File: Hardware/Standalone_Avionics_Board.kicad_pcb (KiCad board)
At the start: 4 copper layers, 112.4 x 57.1 mm, 131 parts, among them J1 GPS_Ant, J2 Charges A/B Terminal, J3 Charges C/D Terminal, J4 RF_Ant, J5 3-Pin Molex Power, J6 10118192-0001LF, J7 ARM 10 Pin, Q1 SI1040X-T1-GE3, Q2 SI7232DN-T1-GE3, Q3 SI7232DN-T1-GE3, U1 Si4463, U10 LM317T, U11 USBLC6-2SC6, U12 STM32L562VET, U13 W25Q32JVSS, U2 Si4463, U3 RSD-897.500-942.500-1612-TR, U4 ADL5521, U5 MS5607-02BA, U6 MAX-8Q, U7 KX134-1211, U8 MCP9808_MSOP, U9 BNO055, Y1 30MHz, Y2 30MHz, Y3 32.768kHz

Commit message: Routed ESD protection chip for USB
I really hate how this connects, I made the chip go on the bottom of the board but I really don't want to
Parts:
- added REF**: PinSocket_1x04_P2.54mm_Vertical, Connector_PinSocket_2.54mm:PinSocket_1x04_P2.54mm_Vertical, F.Cu at (4.42, -6.05)
- added REF**: PinHeader_1x04_P2.54mm_Vertical, Connector_PinHeader_2.54mm:PinHeader_1x04_P2.54mm_Vertical, F.Cu at (4.42, -27.9)
- added REF**: PinHeader_1x05_P2.54mm_Vertical, Connector_PinHeader_2.54mm:PinHeader_1x05_P2.54mm_Vertical, B.Cu at (113.0, 163.3)
- added REF**: PinSocket_1x05_P2.54mm_Vertical, Connector_PinSocket_2.54mm:PinSocket_1x05_P2.54mm_Vertical, B.Cu at (113.0, 141.5)
- added REF**: PinSocket_1x05_P2.54mm_Vertical, Connector_PinSocket_2.54mm:PinSocket_1x05_P2.54mm_Vertical, F.Cu at (113.0, 131.5)
- added REF**: PinHeader_1x05_P2.54mm_Vertical, Connector_PinHeader_2.54mm:PinHeader_1x05_P2.54mm_Vertical, F.Cu at (113.0, 109.7)
- C23, L12, Q1, R2, R3, R4, U11: moved to B.Cu
- Y3: footprint Crystal:Crystal_DS26_D2.0mm_L6.0mm_Horizontal_1EP_style1 -> Crystal:Crystal_SMD_0603-2Pin_6.0x3.5mm
- moved R2 215.7 mm to (99.7, 149.3), turned to 315 degrees
- moved R3 214.8 mm to (103.7, 148.9), turned to 135 degrees
- moved C23 212.6 mm to (104.2, 146.8), turned to 45 degrees
- moved Q1 212.3 mm to (101.3, 146.7), turned to 315 degrees
- moved L12 211.0 mm to (101.5, 149.7), turned to 270 degrees
- moved R4 208.2 mm to (103.3, 145.4), turned to 315 degrees
- moved FB1 112.3 mm to (154.3, 109.1)
- moved C28 87.9 mm to (166.9, 131.1), turned to 180 degrees
- moved C27 87.2 mm to (150.9, 127.9), turned to 180 degrees
- moved C26 85.8 mm to (155.0, 125.2), turned to 180 degrees
- moved C29 76.9 mm to (167.1, 128.2)
- moved J6 65.1 mm to (169.1, 110.5)
- moved U11 46.2 mm to (157.3, 110.1), turned to 0 degrees
- moved Y3 11.1 mm to (163.9, 129.6)
- moved C35 7.81 mm to (142.9, 124.5), turned to 45 degrees
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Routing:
- net /USB, ESD, and Debug/D-: track 0.00 -> 41.0 mm, vias 0 -> 1
- net /USB, ESD, and Debug/D+: track 0.00 -> 40.5 mm, vias 0 -> 1
- net /~GPS_RESET: track 0.00 -> 35.2 mm
- net GND: track 40.3 -> 66.9 mm, vias 10 -> 23
- net /GPS_TX: track 0.00 -> 25.6 mm
- net /GPS_RX: track 0.00 -> 15.4 mm
- net /USB, ESD, and Debug/USB_CONN_D+: track 0.00 -> 13.7 mm, vias 0 -> 1
- net +3V3: track 26.3 -> 39.5 mm, vias 6 -> 8
- net Net-(C28-Pad2): track 0.00 -> 12.5 mm
- net /USB, ESD, and Debug/USB_CONN_D-: track 0.00 -> 11.9 mm, vias 0 -> 1
- net /MAX-8Q/GPS_ANT: track 0.00 -> 11.8 mm
- net Net-(C29-Pad1): track 0.00 -> 11.2 mm
- net /SENSORS_I2C_SDA: track 23.0 -> 31.4 mm
- net /MAX-8Q/GPS_VCC_RF: track 0.00 -> 7.46 mm
- net /SENSORS_I2C_SCL: track 28.3 -> 34.5 mm
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- added copper zone on GND.Cu, net GND

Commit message: All chips on layout besides passives
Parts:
- removed the REF** at (4.42, -6.05)
- removed the REF** at (4.42, -27.9)
- U10: footprint Package_TO_SOT_THT:TO-220-3_Vertical -> Package_TO_SOT_SMD:SOT-223-3_TabPin2
- moved C45 150.5 mm to (146.6, 116.6), turned to 90 degrees
- moved R6 133.9 mm to (157.3, 116.0)
- moved R17 127.7 mm to (173.0, 165.9)
- moved R5 124.1 mm to (159.2, 116.0)
- moved R16 121.4 mm to (139.2, 152.0)
- moved U10 119.2 mm to (156.7, 112.0), turned to 180 degrees
- moved C31 118.6 mm to (163.2, 114.2), turned to 270 degrees
- moved R20 118.3 mm to (173.9, 163.0)
- moved R18 116.0 mm to (170.0, 165.4)
- moved R15 114.3 mm to (172.8, 146.9)
- moved R22 111.8 mm to (168.7, 161.5)
- moved R19 108.4 mm to (168.2, 144.7)
- moved R21 108.3 mm to (179.1, 145.2)
- moved R26 108.3 mm to (163.2, 156.2)
- moved R28 108.3 mm to (176.2, 145.2)
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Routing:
- net +5V: track 0.00 -> 28.0 mm, vias 0 -> 1
- net /USB, ESD, and Debug/D-: track 41.0 -> 16.6 mm
- net /USB, ESD, and Debug/D+: track 40.5 -> 17.9 mm
- net +3V3: track 39.5 -> 60.3 mm, vias 8 -> 12
- net GND: track 66.9 -> 81.8 mm, vias 23 -> 31
- net /FLASH_MOSI: track 0.00 -> 14.0 mm
- net /~FLASH_CS: track 0.00 -> 13.2 mm
- net /GPS_RX: track 15.4 -> 28.2 mm
- net /FLASH_MISO: track 0.00 -> 12.7 mm
- net /USB, ESD, and Debug/USB_CONN_D+: track 13.7 -> 26.1 mm
- net /USB, ESD, and Debug/USB_CONN_D-: track 11.9 -> 24.3 mm
- net /FLASH_CLK: track 0.00 -> 12.1 mm
- net Net-(R5-Pad1): track 0.00 -> 3.12 mm
- net Net-(FB1-Pad2): track 0.00 -> 2.46 mm
- net Net-(D1-Pad2): track 0.00 -> 1.09 mm

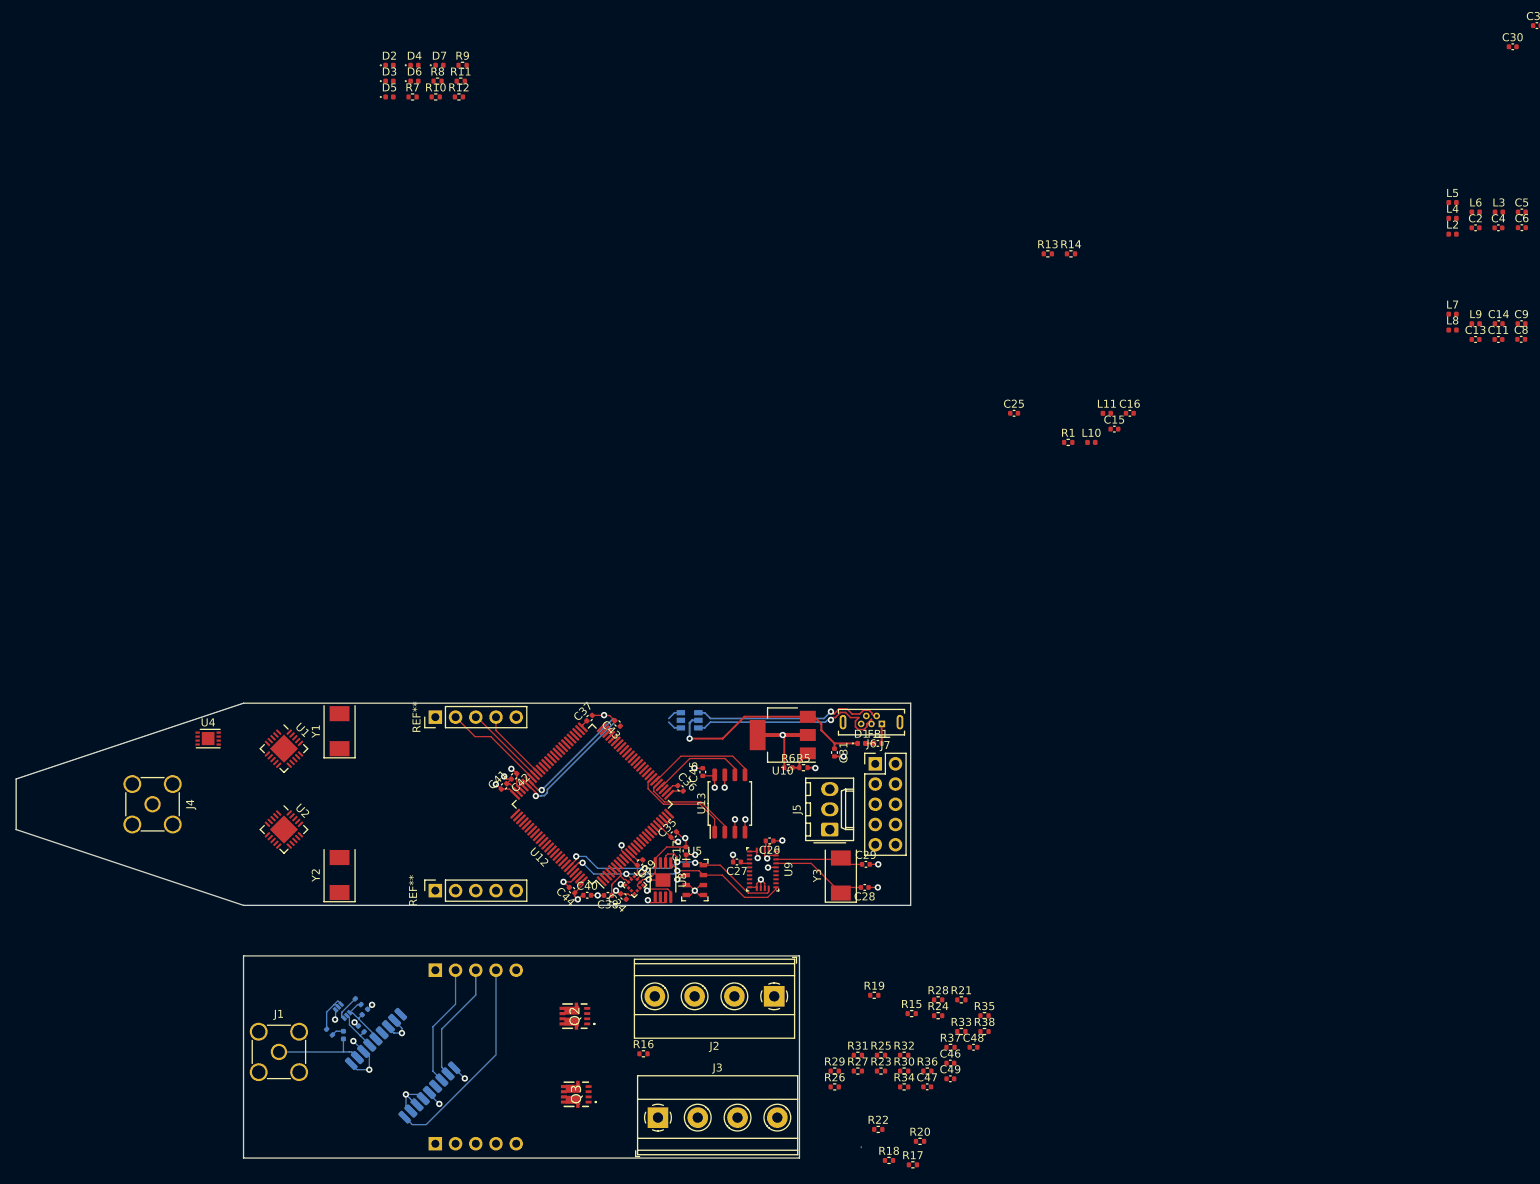
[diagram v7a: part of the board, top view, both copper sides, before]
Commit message: Added Mouse Bites
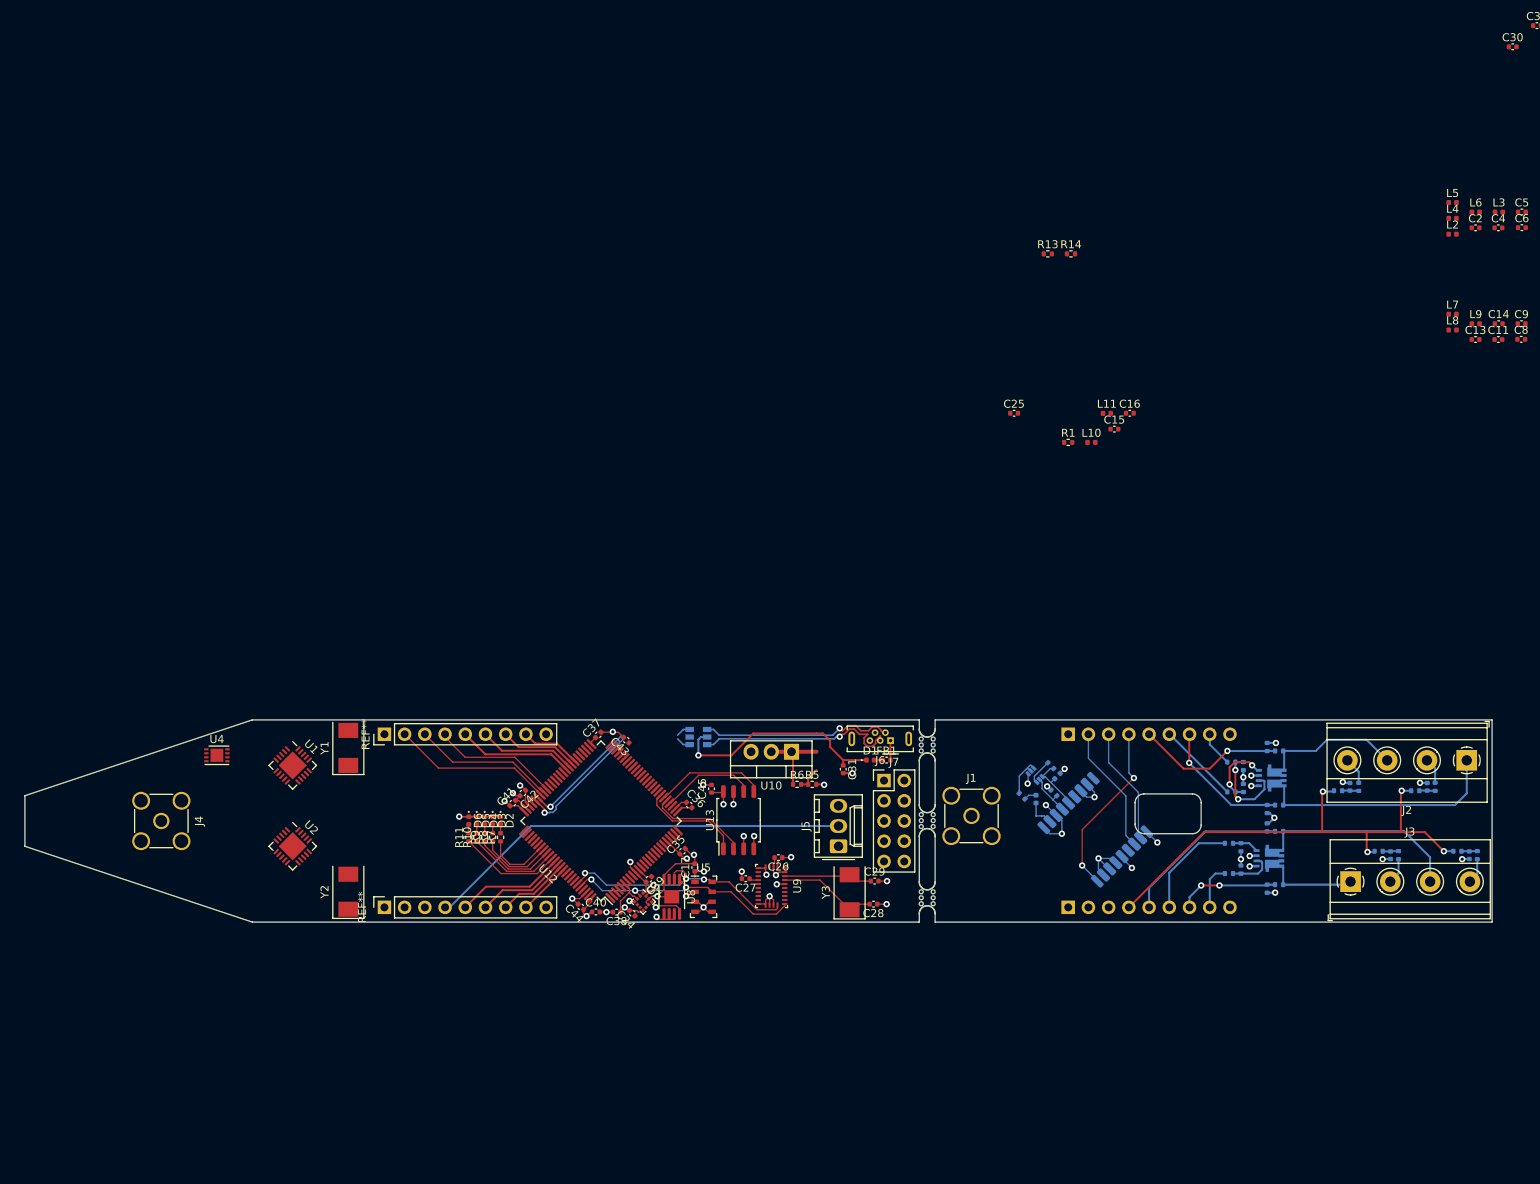
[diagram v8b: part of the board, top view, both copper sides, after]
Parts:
- removed D7: LED, LED_SMD:LED_0402_1005Metric
- removed R12: 100Ω, Resistor_SMD:R_0402_1005Metric
- added mouse-bite-2mm-slot: VAL**, RDT_Custom_Footprints:mouse-bite-2mm-slot, F.Cu at (174.8, 122.7)
- added mouse-bite-2mm-slot: VAL**, RDT_Custom_Footprints:mouse-bite-2mm-slot, F.Cu at (174.8, 132.4)
- added mouse-bite-2mm-slot: VAL**, RDT_Custom_Footprints:mouse-bite-2mm-slot, F.Cu at (174.8, 113.2)
- C46, C47, C48, C49, Q2, Q3, R15, R16, R17, R18, R19, R20, R21, R22, R23, R24, R25, R26, R27, R28, R29, R30, R31, R32, R33, R34, R35, R36, R37, R38: moved to B.Cu
- REF** (x2): value PinHeader_1x05_P2.54mm_Vertical -> PinHeader_1x09_P2.54mm_Vertical; footprint Connector_PinHeader_2.54mm:PinHeader_1x05_P2.54mm_Vertical -> Connector_PinHeader_2.54mm:PinHeader_1x09_P2.54mm_Vertical
- REF** (x2): value PinSocket_1x05_P2.54mm_Vertical -> PinSocket_1x09_P2.54mm_Vertical; footprint Connector_PinSocket_2.54mm:PinSocket_1x05_P2.54mm_Vertical -> Connector_PinSocket_2.54mm:PinSocket_1x09_P2.54mm_Vertical
- U10: footprint Package_TO_SOT_SMD:SOT-223-3_TabPin2 -> Package_TO_SOT_THT:TO-220-3_Vertical
- moved R9 97.0 mm to (119.2, 124.8), turned to 90 degrees
- moved D2 95.9 mm to (121.2, 122.7), turned to 270 degrees
- moved D4 95.3 mm to (119.2, 122.7), turned to 270 degrees
- moved R8 95.3 mm to (120.2, 124.8), turned to 90 degrees
- moved R11 95.0 mm to (117.2, 124.8), turned to 90 degrees
- moved D3 93.8 mm to (120.2, 122.7), turned to 270 degrees
- moved R7 93.7 mm to (121.2, 124.8), turned to 90 degrees
- moved R10 93.2 mm to (118.2, 124.8), turned to 90 degrees
- moved D6 93.2 mm to (117.2, 122.7), turned to 270 degrees
- moved Q2 92.5 mm to (218.0, 117.3)
- moved L12 91.9 mm to (188.5, 120.0)
- moved R2 91.9 mm to (186.7, 119.6)
- moved R3 91.9 mm to (190.7, 119.2)
- moved C23 91.9 mm to (191.2, 117.1)
- moved J1 91.9 mm to (180.4, 122.1)
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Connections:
- REF** pad 4: (no net) -> +5V (x2)
- REF** pad 5: GND -> /Sense_D
- REF** pad 5: GND -> /Sense_B (x2)
- REF** pad 1: (no net) -> GND
- REF** pad 5: (no net) -> /Sense_D
- U12 pad 17: /Fire_C -> Net-(U12-Pad17)
- U12 pad 18: /Sense_C -> Net-(U12-Pad18)
- U12 pad 23: /Fire_D -> Net-(U12-Pad23)
- U12 pad 24: /Sense_D -> Net-(U12-Pad24)
- U12 pad 4: /Fire_A -> Net-(U12-Pad4)
- U12 pad 5: /Sense_A -> Net-(U12-Pad5)
- U12 pad 57: Net-(R7-Pad1) -> /Fire_A
- U12 pad 58: Net-(R8-Pad1) -> /Sense_A
- U12 pad 59: Net-(R9-Pad1) -> /Fire_B
- U12 pad 60: Net-(R10-Pad1) -> /Sense_B
- U12 pad 61: Net-(R11-Pad1) -> Net-(U12-Pad61)
- U12 pad 8: /Fire_B -> Net-(U12-Pad8)
- U12 pad 82: Net-(U12-Pad82) -> Net-(R7-Pad1)
- U12 pad 83: Net-(U12-Pad83) -> Net-(R8-Pad1)
- U12 pad 84: Net-(U12-Pad84) -> Net-(R9-Pad1)
- U12 pad 85: Net-(U12-Pad85) -> Net-(R10-Pad1)
- U12 pad 86: Net-(U12-Pad86) -> Net-(R11-Pad1)
- U12 pad 87: Net-(U12-Pad87) -> /Sense_D
- U12 pad 88: Net-(U12-Pad88) -> /Fire_D
- U12 pad 89: Net-(U12-Pad89) -> /Sense_C
- U12 pad 9: /Sense_B -> Net-(U12-Pad9)
- U12 pad 90: Net-(U12-Pad90) -> /Fire_C
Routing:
- net +5V: track 28.0 -> 143.8 mm, vias 1 -> 5
- net /Sense_D: track 0.00 -> 34.9 mm
- net /Sense_B: track 0.00 -> 33.1 mm, vias 0 -> 1
- net /Charges Firing Circuits/Fet_A+: track 0.00 -> 30.3 mm
- net /Sense_A: track 0.00 -> 26.5 mm, vias 0 -> 1
- net /Charges Firing Circuits/Fet_D+: track 0.00 -> 25.3 mm
- net /Fire_D: track 0.00 -> 24.2 mm
- net /Fire_B: track 0.00 -> 22.6 mm
- net /Sense_C: track 0.00 -> 21.7 mm, vias 0 -> 2
- net GND: track 81.8 -> 102.4 mm, vias 31 -> 45
- net /Charges Firing Circuits/Fet_B+: track 0.00 -> 17.2 mm
- net Net-(R11-Pad1): track 0.00 -> 12.9 mm
- net /Fire_C: track 0.00 -> 12.4 mm
- net /Fire_A: track 0.00 -> 11.9 mm
- net Net-(R10-Pad1): track 0.00 -> 11.5 mm
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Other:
- board size 112.4 x 57.1 mm -> 184.3 x 25.4 mm
